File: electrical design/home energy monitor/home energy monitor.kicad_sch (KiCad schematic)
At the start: 26 parts, among them J4 Conn_01x07_Socket, J5 Conn_01x07_Socket

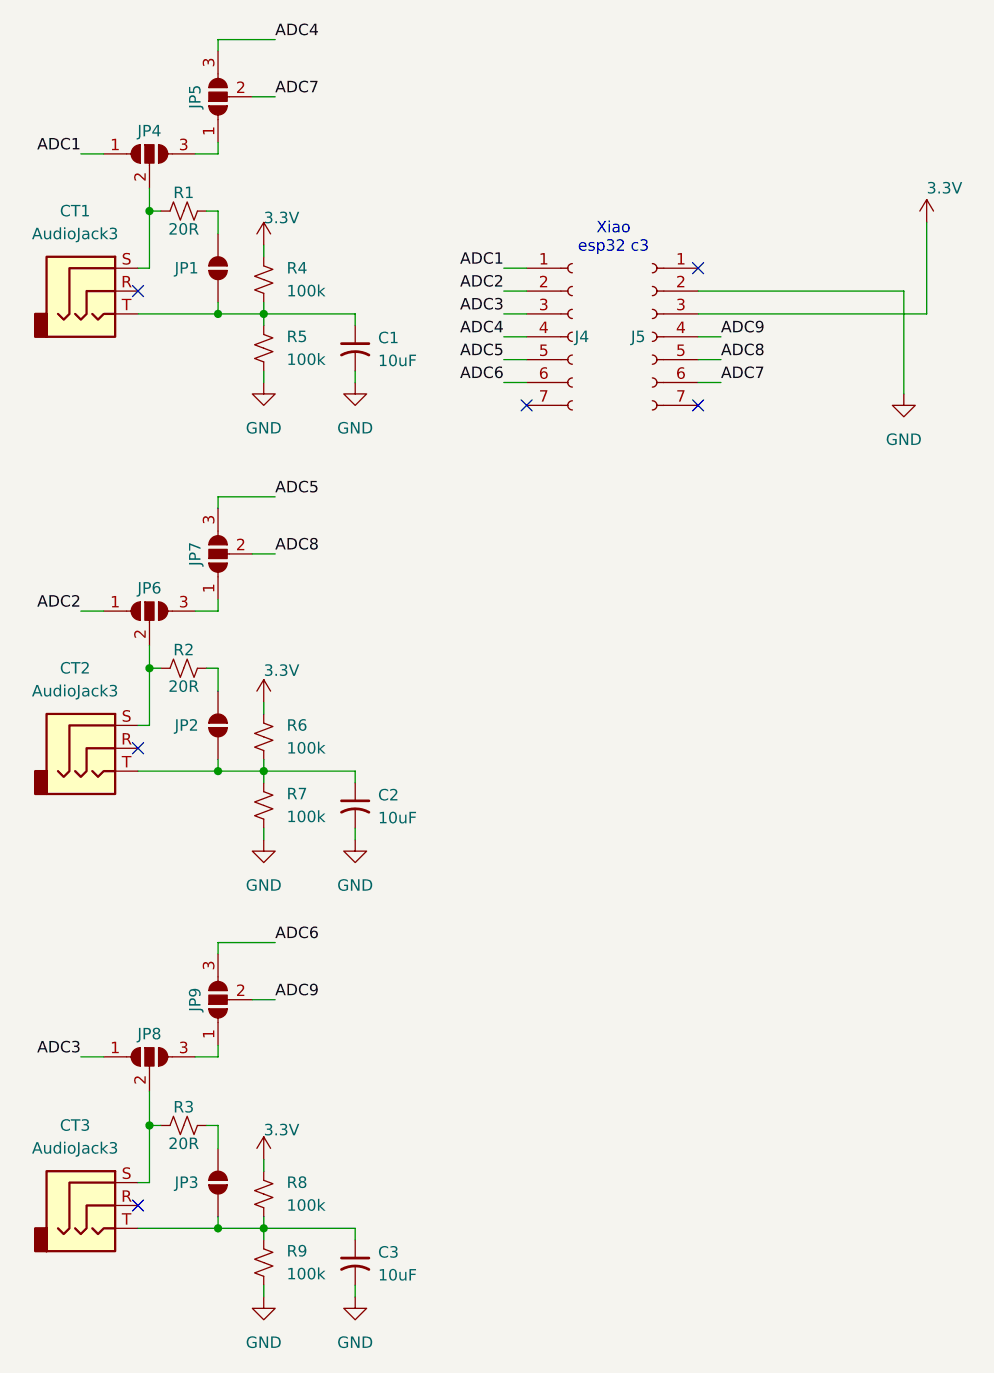
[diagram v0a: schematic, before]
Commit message: Added PCB routing for alternate ADC pins
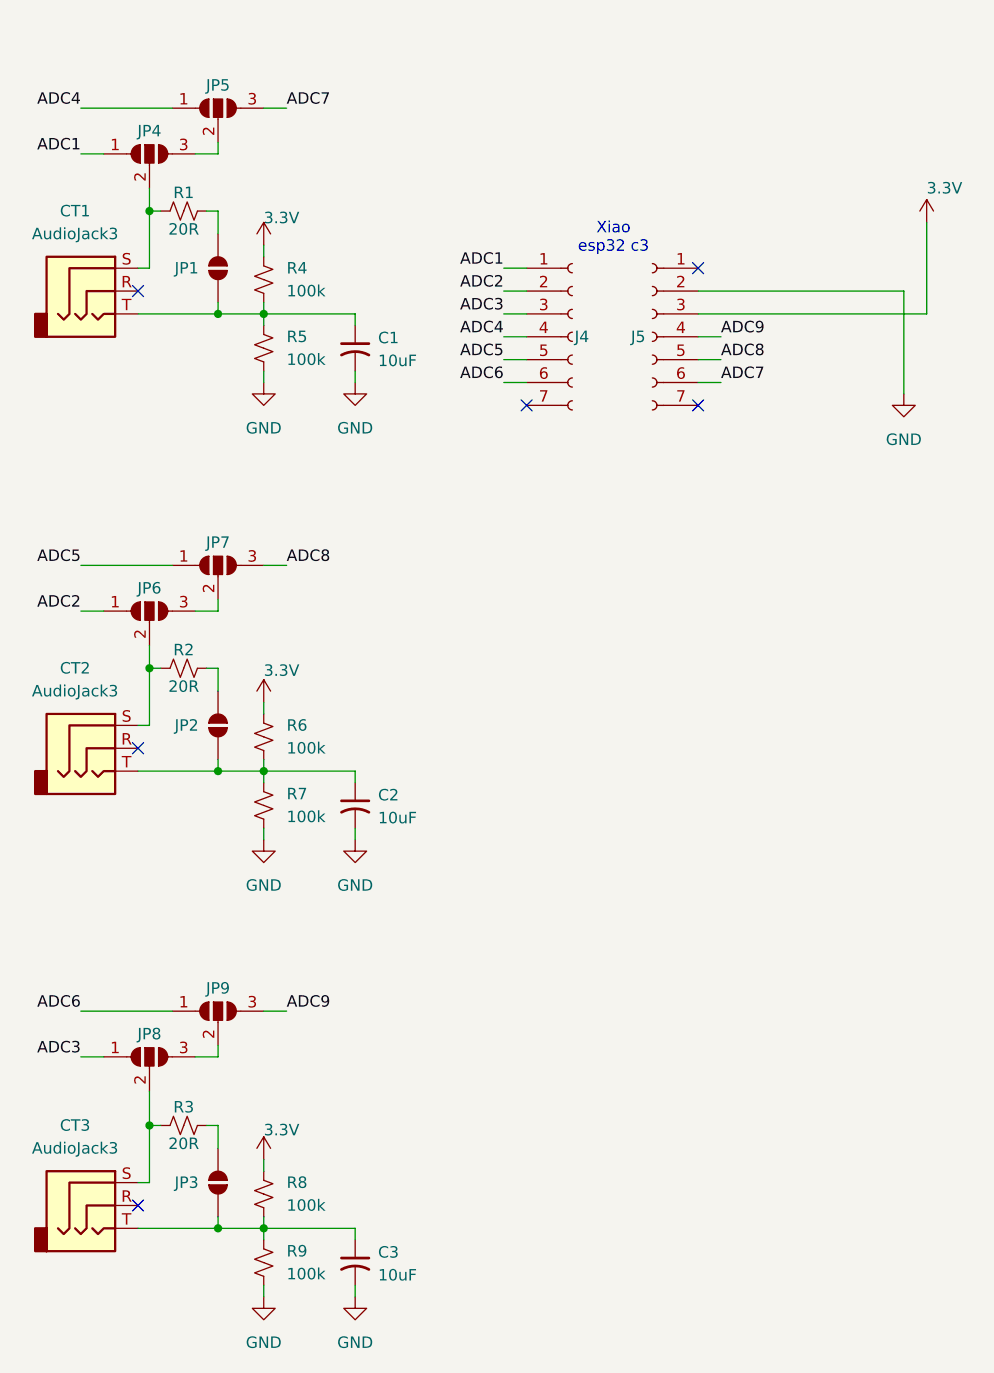
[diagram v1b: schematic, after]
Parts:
- JP4, JP5, JP6, JP7, JP8, JP9: footprint (none) -> Jumper:SolderJumper-3_P1.3mm_Open_RoundedPad1.0x1.5mm_NumberLabels
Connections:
- net ADC4: now also JP5.1 (A); no longer JP5.3 (B)
- net ADC5: now also JP7.1 (A); no longer JP7.3 (B)
- net ADC6: now also JP9.1 (A); no longer JP9.3 (B)
- net ADC7: now also JP5.3 (B); no longer JP5.2 (C)
- net ADC8: now also JP7.3 (B); no longer JP7.2 (C)
- net ADC9: now also JP9.3 (B); no longer JP9.2 (C)
- net at JP6.3 (B): now also JP7.2 (C); no longer JP7.1 (A)
- net at JP4.3 (B): now also JP5.2 (C); no longer JP5.1 (A)
- net at JP8.3 (B): now also JP9.2 (C); no longer JP9.1 (A)
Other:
- moved on the sheet: JP5, JP7, JP9
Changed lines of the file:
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@@
 	(wire
 		(pts
-			(xy 45.72 118.11) (xy 52.07 118.11)
-		)
-		(stroke
-			(width 0)
-			(type default)
-		)
-	)
-	(wire
-		(pts
 			(xy 36.83 93.98) (xy 38.1 93.98)
 		)
@@
 	(wire
 		(pts
-			(xy 45.72 17.78) (xy 52.07 17.78)
+			(xy 40.64 25.4) (xy 30.48 25.4)
 		)
 		(stroke
@@
 	(wire
 		(pts
-			(xy 45.72 68.58) (xy 52.07 68.58)
-		)
-		(stroke
-			(width 0)
-			(type default)
-		)
-	)
-	(wire
-		(pts
 			(xy 30.48 30.48) (xy 33.02 30.48)
 		)
@@
 	(wire
 		(pts
-			(xy 38.1 34.29) (xy 38.1 36.83)
+			(xy 30.48 76.2) (xy 40.64 76.2)
 		)
 		(stroke
@@
 	(wire
 		(pts
-			(xy 50.8 149.86) (xy 50.8 148.59)
+			(xy 38.1 34.29) (xy 38.1 36.83)
 		)
 		(stroke
@@
 	(wire
 		(pts
-			(xy 77.47 53.34) (xy 80.01 53.34)
+			(xy 50.8 149.86) (xy 50.8 148.59)
 		)
 		(stroke
@@
 	(wire
 		(pts
-			(xy 45.72 119.38) (xy 45.72 118.11)
+			(xy 77.47 53.34) (xy 80.01 53.34)
 		)
 		(stroke
@@
 	(wire
 		(pts
-			(xy 45.72 69.85) (xy 45.72 68.58)
-		)
-		(stroke
-			(width 0)
-			(type default)
-		)
-	)
-	(wire
-		(pts
 			(xy 39.37 87.63) (xy 38.1 87.63)
 		)
@@
 	(wire
 		(pts
-			(xy 49.53 124.46) (xy 52.07 124.46)
+			(xy 50.8 125.73) (xy 53.34 125.73)
 		)
 		(stroke
@@
 	(wire
 		(pts
-			(xy 49.53 74.93) (xy 52.07 74.93)
+			(xy 50.8 76.2) (xy 53.34 76.2)
 		)
 		(stroke
@@
 	(wire
 		(pts
-			(xy 45.72 19.05) (xy 45.72 17.78)
-		)
-		(stroke
-			(width 0)
-			(type default)
-		)
-	)
-	(wire
-		(pts
-			(xy 49.53 24.13) (xy 52.07 24.13)
+			(xy 50.8 25.4) (xy 53.34 25.4)
 		)
 		(stroke
@@
 		)
 	)
+	(wire
+		(pts
+			(xy 30.48 125.73) (xy 40.64 125.73)
+		)
+		(stroke
+			(width 0)
+			(type default)
+		)
+	)
 	(label "ADC3"
 		(at 30.48 130.81 180)
@@
 	)
 	(label "ADC4"
-		(at 52.07 17.78 0)
+		(at 30.48 25.4 180)
 		(effects
 			(font
 				(size 1.27 1.27)
 			)
-			(justify left bottom)
+			(justify right bottom)
 		)
 	)
@@
 	)
 	(label "ADC7"
-		(at 52.07 24.13 0)
+		(at 53.34 25.4 0)
 		(effects
 			(font
@@
 	)
 	(label "ADC8"
-		(at 52.07 74.93 0)
+		(at 53.34 76.2 0)
 		(effects
 			(font
@@
 	)
 	(label "ADC6"
-		(at 52.07 118.11 0)
+		(at 30.48 125.73 180)
 		(effects
 			(font
 				(size 1.27 1.27)
 			)
-			(justify left bottom)
+			(justify right bottom)
 		)
 	)
@@
 	)
 	(label "ADC5"
-		(at 52.07 68.58 0)
+		(at 30.48 76.2 180)
 		(effects
 			(font
 				(size 1.27 1.27)
 			)
-			(justify left bottom)
+			(justify right bottom)
 		)
 	)
@@
 	)
 	(label "ADC9"
-		(at 52.07 124.46 0)
+		(at 53.34 125.73 0)
 		(effects
 			(font
@@
 	(symbol
 		(lib_id "Jumper:SolderJumper_3_Open")
-		(at 45.72 74.93 90)
+		(at 45.72 76.2 0)
 		(unit 1)
 		(exclude_from_sim no)
@@
 		(dnp no)
 		(property "Reference" "JP7"
-			(at 43.18 74.93 0)
+			(at 45.72 73.66 0)
 			(effects
 				(font
@@
 		)
 		(property "Value" "SolderJumper_3_Open"
-			(at 41.91 74.93 0)
+			(at 45.72 72.39 0)
 			(effects
 				(font
@@
 			)
 		)
-		(property "Footprint" ""
-			(at 45.72 74.93 0)
+		(property "Footprint" "Jumper:SolderJumper-3_P1.3mm_Open_RoundedPad1.0x1.5mm_NumberLabels"
+			(at 45.72 76.2 0)
 			(effects
 				(font
@@
 		)
 		(property "Datasheet" "~"
-			(at 45.72 74.93 0)
+			(at 45.72 76.2 0)
 			(effects
 				(font
@@
 		)
 		(property "Description" "Solder Jumper, 3-pole, open"
-			(at 45.72 74.93 0)
+			(at 45.72 76.2 0)
 			(effects
 				(font
@@
 			)
 		)
-		(property "Footprint" ""
+		(property "Footprint" "Jumper:SolderJumper-3_P1.3mm_Open_RoundedPad1.0x1.5mm_NumberLabels"
 			(at 38.1 81.28 0)
 			(effects
@@
 	(symbol
 		(lib_id "Jumper:SolderJumper_3_Open")
-		(at 45.72 24.13 90)
+		(at 45.72 25.4 0)
 		(unit 1)
 		(exclude_from_sim no)
@@
 		(dnp no)
 		(property "Reference" "JP5"
-			(at 43.18 24.13 0)
+			(at 45.72 22.86 0)
 			(effects
 				(font
@@
 		)
 		(property "Value" "SolderJumper_3_Open"
-			(at 41.91 24.13 0)
+			(at 45.72 21.59 0)
 			(effects
 				(font
@@
 			)
 		)
-		(property "Footprint" ""
-			(at 45.72 24.13 0)
+		(property "Footprint" "Jumper:SolderJumper-3_P1.3mm_Open_RoundedPad1.0x1.5mm_NumberLabels"
+			(at 45.72 25.4 0)
 			(effects
 				(font
@@
 		)
 		(property "Datasheet" "~"
-			(at 45.72 24.13 0)
+			(at 45.72 25.4 0)
 			(effects
 				(font
@@
 		)
 		(property "Description" "Solder Jumper, 3-pole, open"
-			(at 45.72 24.13 0)
+			(at 45.72 25.4 0)
 			(effects
 				(font
@@
 	(symbol
 		(lib_id "Jumper:SolderJumper_3_Open")
-		(at 45.72 124.46 90)
+		(at 45.72 125.73 0)
 		(unit 1)
 		(exclude_from_sim no)
@@
 		(dnp no)
 		(property "Reference" "JP9"
-			(at 43.18 124.46 0)
+			(at 45.72 123.19 0)
 			(effects
 				(font
@@
 		)
 		(property "Value" "SolderJumper_3_Open"
-			(at 41.91 124.46 0)
+			(at 45.72 121.92 0)
 			(effects
 				(font
@@
 			)
 		)
-		(property "Footprint" ""
-			(at 45.72 124.46 0)
+		(property "Footprint" "Jumper:SolderJumper-3_P1.3mm_Open_RoundedPad1.0x1.5mm_NumberLabels"
+			(at 45.72 125.73 0)
 			(effects
 				(font
@@
 		)
 		(property "Datasheet" "~"
-			(at 45.72 124.46 0)
+			(at 45.72 125.73 0)
 			(effects
 				(font
@@
 		)
 		(property "Description" "Solder Jumper, 3-pole, open"
-			(at 45.72 124.46 0)
+			(at 45.72 125.73 0)
 			(effects
 				(font
@@
 			)
 		)
-		(property "Footprint" ""
+		(property "Footprint" "Jumper:SolderJumper-3_P1.3mm_Open_RoundedPad1.0x1.5mm_NumberLabels"
 			(at 38.1 30.48 0)
 			(effects
@@
 			)
 		)
-		(property "Footprint" ""
+		(property "Footprint" "Jumper:SolderJumper-3_P1.3mm_Open_RoundedPad1.0x1.5mm_NumberLabels"
 			(at 38.1 130.81 0)
 			(effects
